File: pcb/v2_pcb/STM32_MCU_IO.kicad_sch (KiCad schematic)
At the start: 24 parts, among them U1 STM32N657X0H3Q

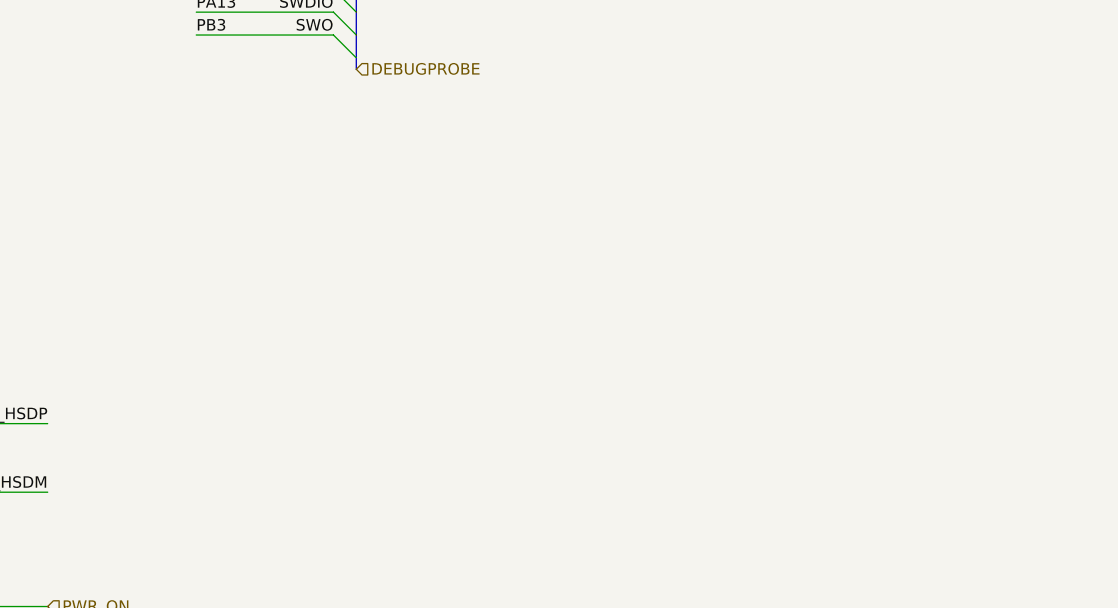
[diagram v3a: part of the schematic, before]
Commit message: add usb to schematic
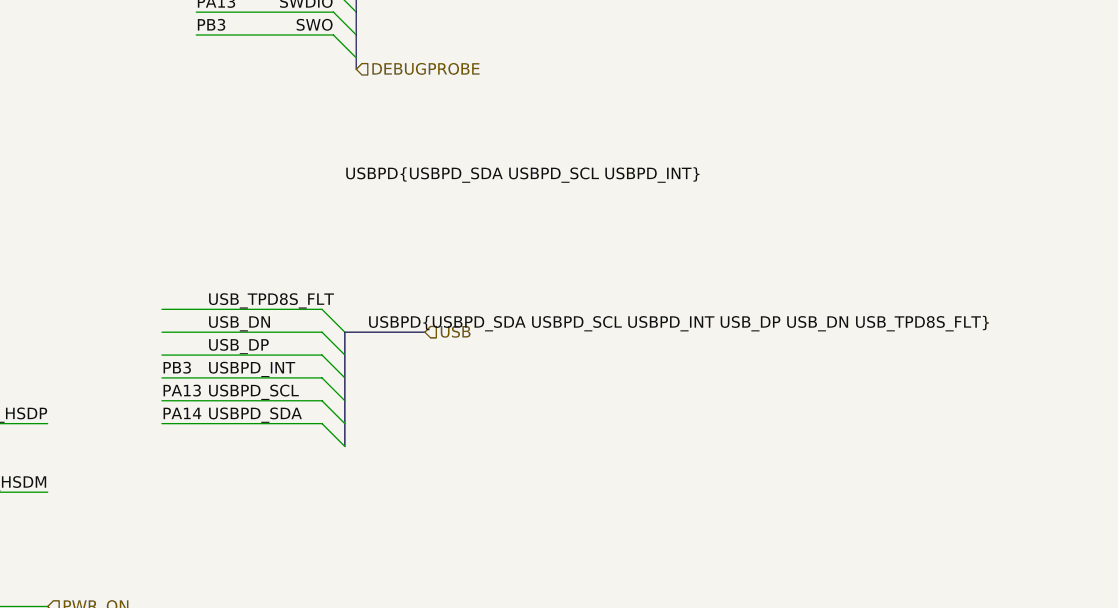
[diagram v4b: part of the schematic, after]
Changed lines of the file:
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@@
 	)
 	(bus_entry
+		(at 317.5 187.96)
+		(size -2.54 -2.54)
+		(stroke
+			(width 0)
+			(type default)
+		)
+	)
+	(bus_entry
 		(at 320.04 93.98)
 		(size 2.54 2.54)
@@
 	)
 	(bus_entry
+		(at 317.5 182.88)
+		(size -2.54 -2.54)
+		(stroke
+			(width 0)
+			(type default)
+		)
+	)
+	(bus_entry
 		(at 320.04 68.58)
 		(size 2.54 2.54)
@@
 	)
 	(bus_entry
+		(at 317.5 190.5)
+		(size -2.54 -2.54)
+		(stroke
+			(width 0)
+			(type default)
+		)
+	)
+	(bus_entry
 		(at 320.04 96.52)
 		(size 2.54 2.54)
@@
 	)
 	(bus_entry
+		(at 317.5 180.34)
+		(size -2.54 -2.54)
+		(stroke
+			(width 0)
+			(type default)
+		)
+	)
+	(bus_entry
 		(at 320.04 81.28)
 		(size 2.54 2.54)
@@
 	)
 	(bus_entry
+		(at 317.5 177.8)
+		(size -2.54 -2.54)
+		(stroke
+			(width 0)
+			(type default)
+		)
+	)
+	(bus_entry
 		(at 316.23 142.24)
 		(size 2.54 2.54)
@@
 	)
 	(bus_entry
+		(at 317.5 185.42)
+		(size -2.54 -2.54)
+		(stroke
+			(width 0)
+			(type default)
+		)
+	)
+	(bus_entry
 		(at 320.04 106.68)
 		(size 2.54 2.54)
@@
 		)
 	)
+	(bus
+		(pts
+			(xy 317.5 190.5) (xy 317.5 177.8)
+		)
+		(stroke
+			(width 0)
+			(type default)
+		)
+	)
 	(wire
 		(pts
@@
 		)
 	)
+	(bus
+		(pts
+			(xy 326.39 177.8) (xy 317.5 177.8)
+		)
+		(stroke
+			(width 0)
+			(type default)
+		)
+	)
 	(wire
 		(pts
@@
 	(wire
 		(pts
+			(xy 297.18 182.88) (xy 314.96 182.88)
+		)
+		(stroke
+			(width 0)
+			(type default)
+		)
+	)
+	(wire
+		(pts
 			(xy 320.04 81.28) (xy 309.88 81.28)
 		)
@@
 	(wire
 		(pts
+			(xy 297.18 175.26) (xy 314.96 175.26)
+		)
+		(stroke
+			(width 0)
+			(type default)
+		)
+	)
+	(wire
+		(pts
 			(xy 72.39 101.6) (xy 85.09 101.6)
 		)
@@
 	(wire
 		(pts
+			(xy 297.18 185.42) (xy 314.96 185.42)
+		)
+		(stroke
+			(width 0)
+			(type default)
+		)
+	)
+	(wire
+		(pts
 			(xy 309.88 66.04) (xy 320.04 66.04)
 		)
@@
 	(wire
 		(pts
+			(xy 297.18 177.8) (xy 314.96 177.8)
+		)
+		(stroke
+			(width 0)
+			(type default)
+		)
+	)
+	(wire
+		(pts
 			(xy 146.05 63.5) (xy 158.75 63.5)
 		)
@@
 	(wire
 		(pts
+			(xy 297.18 187.96) (xy 314.96 187.96)
+		)
+		(stroke
+			(width 0)
+			(type default)
+		)
+	)
+	(wire
+		(pts
 			(xy 142.24 177.8) (xy 154.94 177.8)
 		)
@@
 	(wire
 		(pts
+			(xy 297.18 180.34) (xy 314.96 180.34)
+		)
+		(stroke
+			(width 0)
+			(type default)
+		)
+	)
+	(wire
+		(pts
 			(xy 320.04 109.22) (xy 309.88 109.22)
 		)
@@
 		)
 	)
+	(label "PB3"
+		(at 297.18 182.88 0)
+		(effects
+			(font
+				(size 1.27 1.27)
+			)
+			(justify left bottom)
+		)
+	)
 	(label "PF11"
 		(at 73.66 233.68 0)
@@
 		)
 	)
+	(label "USBPD_INT"
+		(at 302.26 182.88 0)
+		(effects
+			(font
+				(size 1.27 1.27)
+			)
+			(justify left bottom)
+		)
+	)
 	(label "PP5"
 		(at 292.1 93.98 0)
@@
 		)
 	)
+	(label "USBPD_SCL"
+		(at 302.26 185.42 0)
+		(effects
+			(font
+				(size 1.27 1.27)
+			)
+			(justify left bottom)
+		)
+	)
 	(label "PF12"
 		(at 73.66 236.22 0)
@@
 		)
 	)
+	(label "PA14"
+		(at 297.18 187.96 0)
+		(effects
+			(font
+				(size 1.27 1.27)
+			)
+			(justify left bottom)
+		)
+	)
 	(label "PE0"
 		(at 73.66 162.56 0)
@@
 		)
 	)
+	(label "USBPD_SDA"
+		(at 302.26 187.96 0)
+		(effects
+			(font
+				(size 1.27 1.27)
+			)
+			(justify left bottom)
+		)
+	)
 	(label "PP4"
 		(at 259.08 93.98 180)
@@
 		)
 	)
+	(label "USB_DP"
+		(at 302.26 180.34 0)
+		(effects
+			(font
+				(size 1.27 1.27)
+			)
+			(justify left bottom)
+		)
+	)
 	(label "PB3"
 		(at 300.99 144.78 0)
@@
 		)
 	)
+	(label "USBPD{USBPD_SDA USBPD_SCL USBPD_INT USB_DP USB_DN USB_TPD8S_FLT}"
+		(at 320.04 177.8 0)
+		(effects
+			(font
+				(size 1.27 1.27)
+			)
+			(justify left bottom)
+		)
+	)
 	(label "PD1"
 		(at 158.75 78.74 180)
@@
 		)
 	)
+	(label "USBPD{USBPD_SDA USBPD_SCL USBPD_INT}"
+		(at 317.5 161.29 0)
+		(effects
+			(font
+				(size 1.27 1.27)
+			)
+			(justify left bottom)
+		)
+	)
 	(label "OTG1_HSDP"
 		(at 284.48 187.96 180)
@@
 		)
 	)
+	(label "PA13"
+		(at 297.18 185.42 0)
+		(effects
+			(font
+				(size 1.27 1.27)
+			)
+			(justify left bottom)
+		)
+	)
 	(label "PQ4"
 		(at 259.08 50.8 180)
@@
 		)
 	)
+	(label "USB_DN"
+		(at 302.26 177.8 0)
+		(effects
+			(font
+				(size 1.27 1.27)
+			)
+			(justify left bottom)
+		)
+	)
 	(label "PP6"
 		(at 259.08 88.9 180)
@@
 		)
 	)
+	(label "USB_TPD8S_FLT"
+		(at 302.26 175.26 0)
+		(effects
+			(font
+				(size 1.27 1.27)
+			)
+			(justify left bottom)
+		)
+	)
 	(label "PF7"
 		(at 73.66 223.52 0)
@@
 		)
 	)
+	(hierarchical_label "USB"
+		(shape input)
+		(at 326.39 177.8 0)
+		(effects
+			(font
+				(size 1.27 1.27)
+			)
+			(justify left)
+		)
+	)
